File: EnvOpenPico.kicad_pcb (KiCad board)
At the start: 2 copper layers, 21.1 x 51.3 mm, 37 parts, among them J2 B3U-1000P, J3 2.54mm header 01x20, J4 2.54mm header 01x20, J5 Conn_01x03_Male, U1 SPX3819M5-L-3-3, U3 RP2040, X1 XO 32 12Mhz 3225 seiko

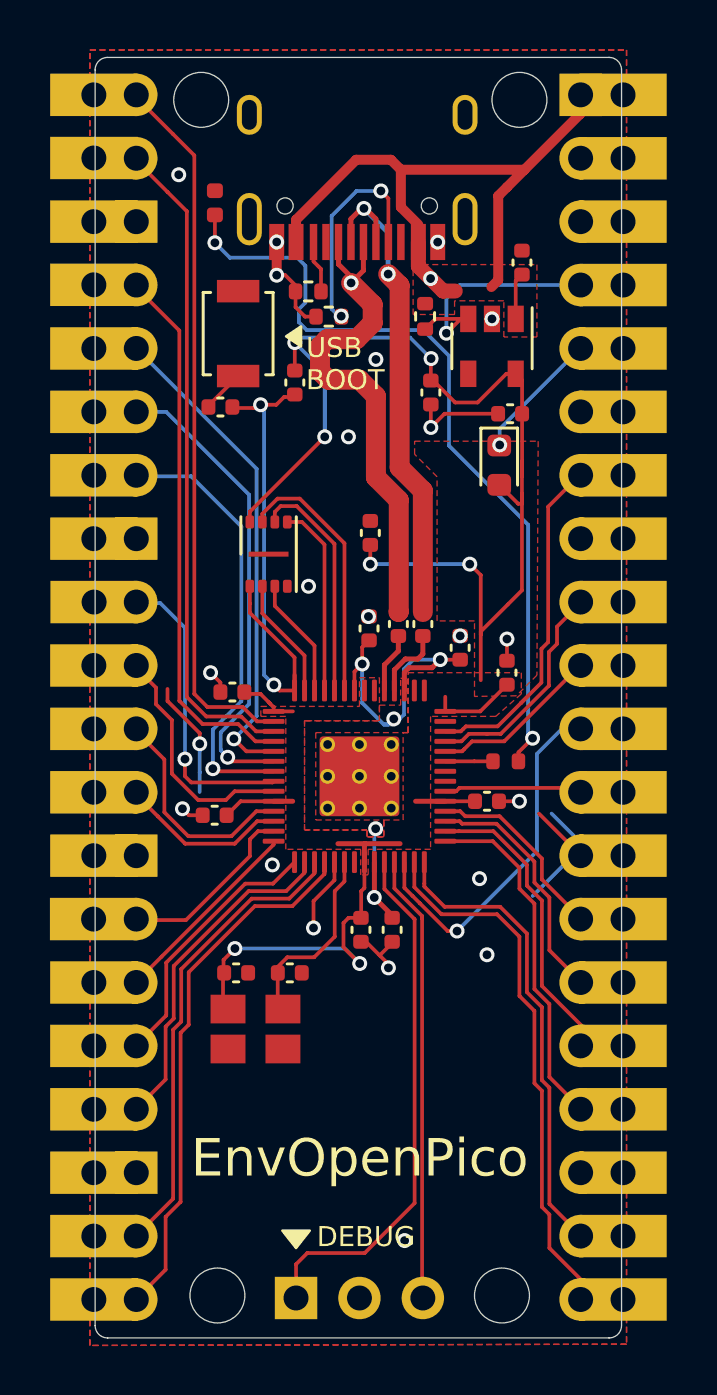
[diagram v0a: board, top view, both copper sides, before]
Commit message: unsure if permanent but can get a hold of components RPI Pico uses
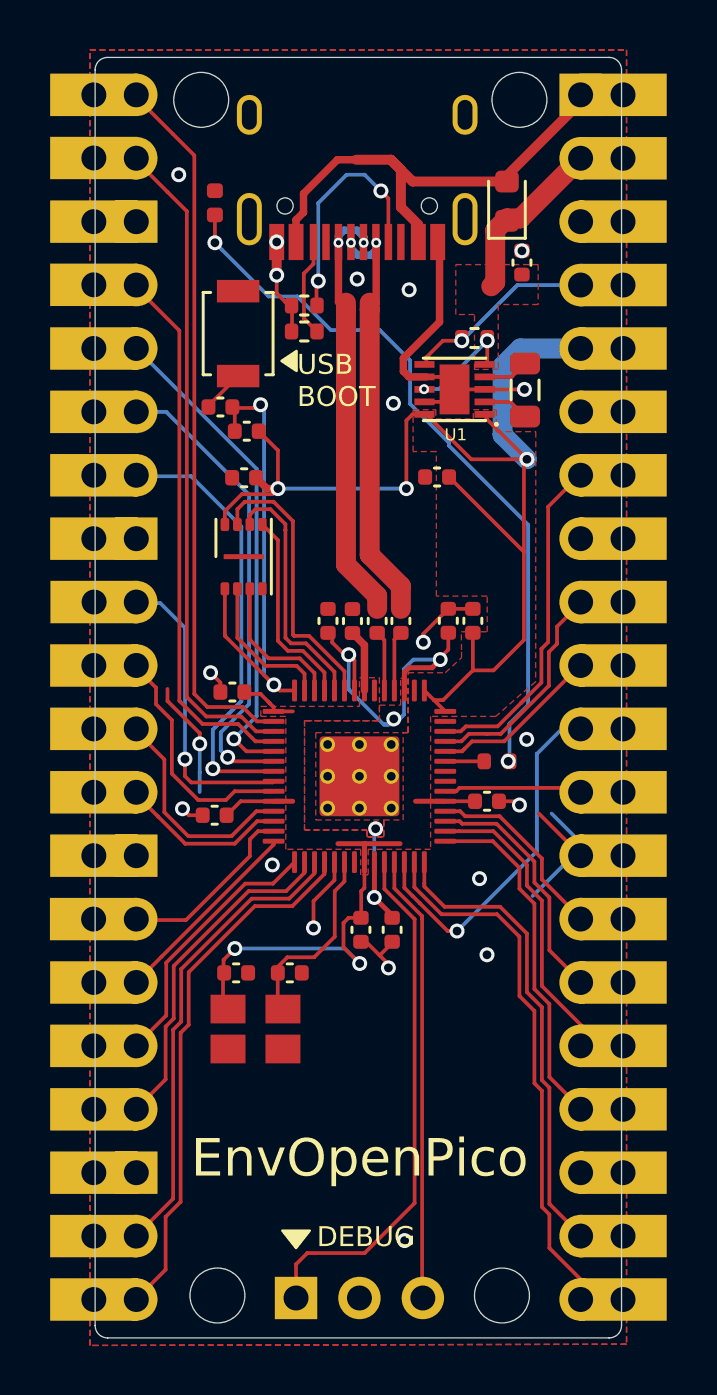
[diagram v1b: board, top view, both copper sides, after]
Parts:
- removed D2: 0603 Diode 1N58, Diode_SMD:D_0603_1608Metric
- added D1: SCHOTTKY DIODE, Diode_SMD:D_0603_1608Metric, F.Cu at (109.6, 63.0)
- added L1: Inductor 2.2uh, Inductor_SMD:L_0805_2012Metric, F.Cu at (110.3, 70.5)
- C1, C17, C4: value 10u -> 10uf 0402
- C10, C3: value 1u -> 1uf 0402
- C11, C13, C14, C15, C5, C6, C7, C8: value 100n -> 100nf 0402
- C2: value 15p -> 15pf 0402
- FLASH1: value W25Q128JVPIQ -> W25Q16JVUXIQ
- R1: value 1k -> 1k Resistor
- R8: value 470 -> 470 ohm resistor
- U1: value SPX3819M5-L-3-3 -> RT6150B-33GQW; footprint Package_TO_SOT_SMD:SOT-23-5 -> RT6150B-33GQW:SON50P250X250X80-11N
- moved C8 9.68 mm to (103.4, 79.8), turned to 90 degrees
- moved C5 5.52 mm to (99.1, 74.1), turned to 180 degrees
- moved C4 3.87 mm to (106.8, 74.0)
- moved R2 2.74 mm to (99.2, 72.2), turned to 180 degrees
- moved C10 2.49 mm to (108.2, 79.8)
- moved U1 2.29 mm to (107.5, 70.5), turned to 180 degrees
- moved R7 2.16 mm to (108.3, 68.5), turned to 180 degrees
- moved C3 1.67 mm to (102.4, 79.8)
- moved R6 1.61 mm to (101.5, 68.2)
- moved C7 1.18 mm to (107.2, 79.8)
- moved R5 1.08 mm to (101.5, 67.2)
- moved FLASH1 1.00 mm to (99.0, 77.2)
- moved R4 0.89 mm to (105.3, 79.8)
- moved R3 0.86 mm to (104.4, 79.8)
- moved R8 0.35 mm to (109.2, 85.4)
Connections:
- J4 pad 2: (no net) -> VBUS
- J4 pad 5: Net-(D2-Pad1) -> +3V3
- J4 pad 6: (no net) -> Net-(J4-Pad6)
- U1 pad 1: VBUS -> +3V3
- U1 pad 2: GND -> Net-(L1-Pad1)
- U1 pad 3: 3V3_EN -> GND
- U1 pad 4: (no net) -> Net-(L1-Pad2)
- U1 pad 5: +3V3 -> VBUS
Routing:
- net GND: track 28.8 -> 39.0 mm, vias 22 -> 20
- net Net-(D2-Pad1): track 5.20 -> 0.00 mm, vias 1 -> 0
- net /USB_D+: track 20.8 -> 17.3 mm, vias 1 -> 2
- net /USB_D-: track 20.3 -> 17.3 mm
- net Net-(D3-Pad2): track 31.9 -> 29.2 mm
- net 3V3_EN: track 10.6 -> 8.26 mm
- net VBUS: track 29.4 -> 31.5 mm, vias 1 -> 2
- net Net-(R6-Pad2): track 2.11 -> 3.98 mm
- net +3V3: track 73.7 -> 75.6 mm, vias 7 -> 5
- net Net-(L1-Pad1): track 0.00 -> 1.79 mm
- net Net-(L1-Pad2): track 0.00 -> 1.77 mm
- net +1V1: track 18.5 -> 19.9 mm
- net /QSPI_SS: track 20.5 -> 19.2 mm
- net /QSPI_SD2: track 4.83 -> 5.88 mm
- net /QSPI_SD1: track 4.88 -> 5.92 mm
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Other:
- rule via_min_size: 0.6 -> 0.4
- board text removed: "3.3V_EN is not implemented"
- board text removed: "VSYS is not implemented"

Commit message: Added some vias and tweaked some placements and adjustments
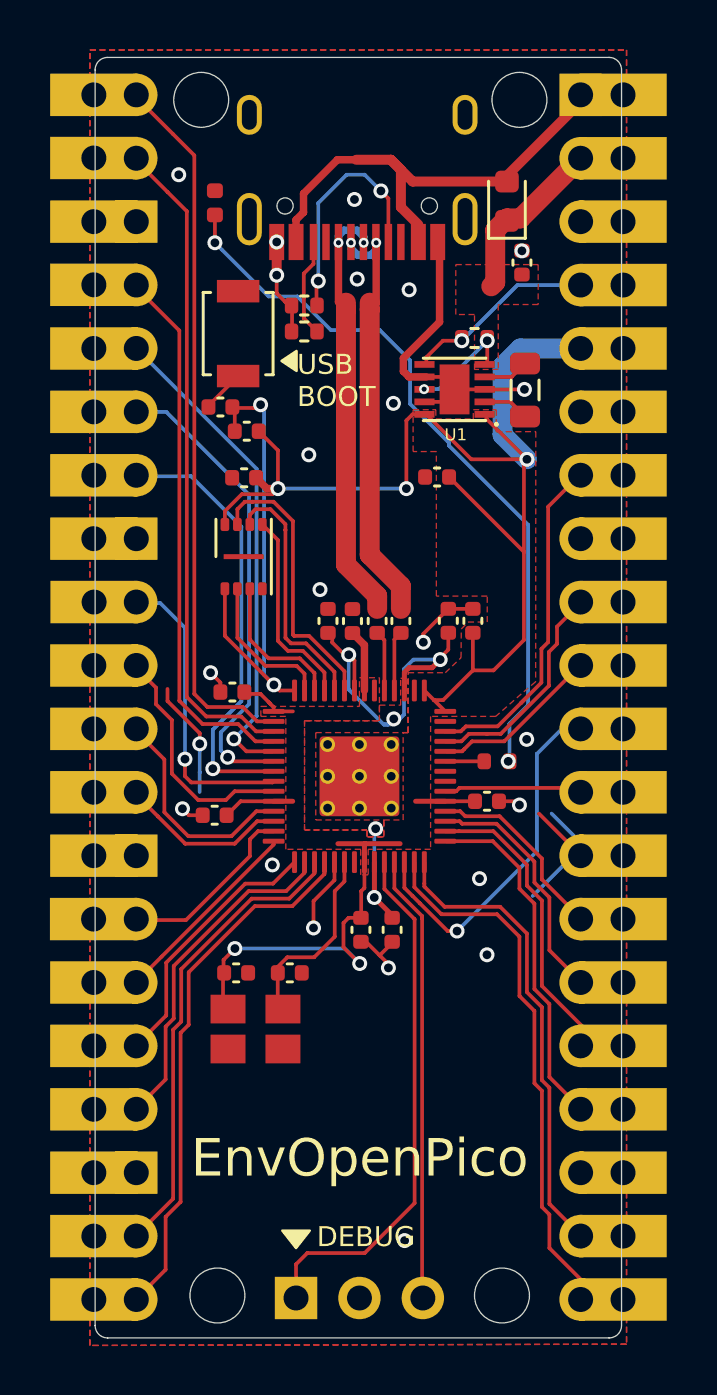
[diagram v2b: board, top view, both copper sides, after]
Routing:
- net GND: vias 20 -> 23

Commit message: Changed out some parts and added more details to their BOM comments
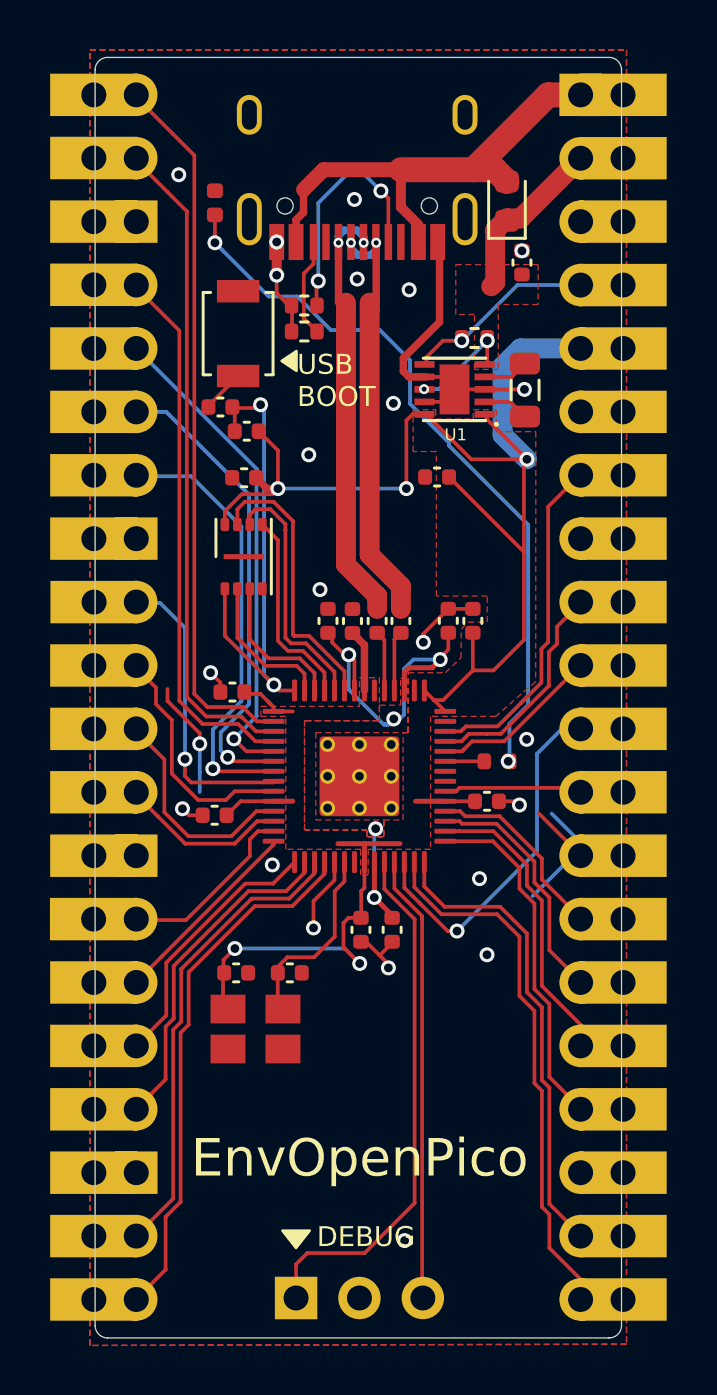
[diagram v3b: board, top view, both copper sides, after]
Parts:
- removed H1, H2, H3, H4: MountingHole, MountingHole:MountingHole_2.2mm_M2
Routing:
- net VBUS: track 31.5 -> 32.1 mm

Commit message: Swapped RT6150GQW for TPS63002
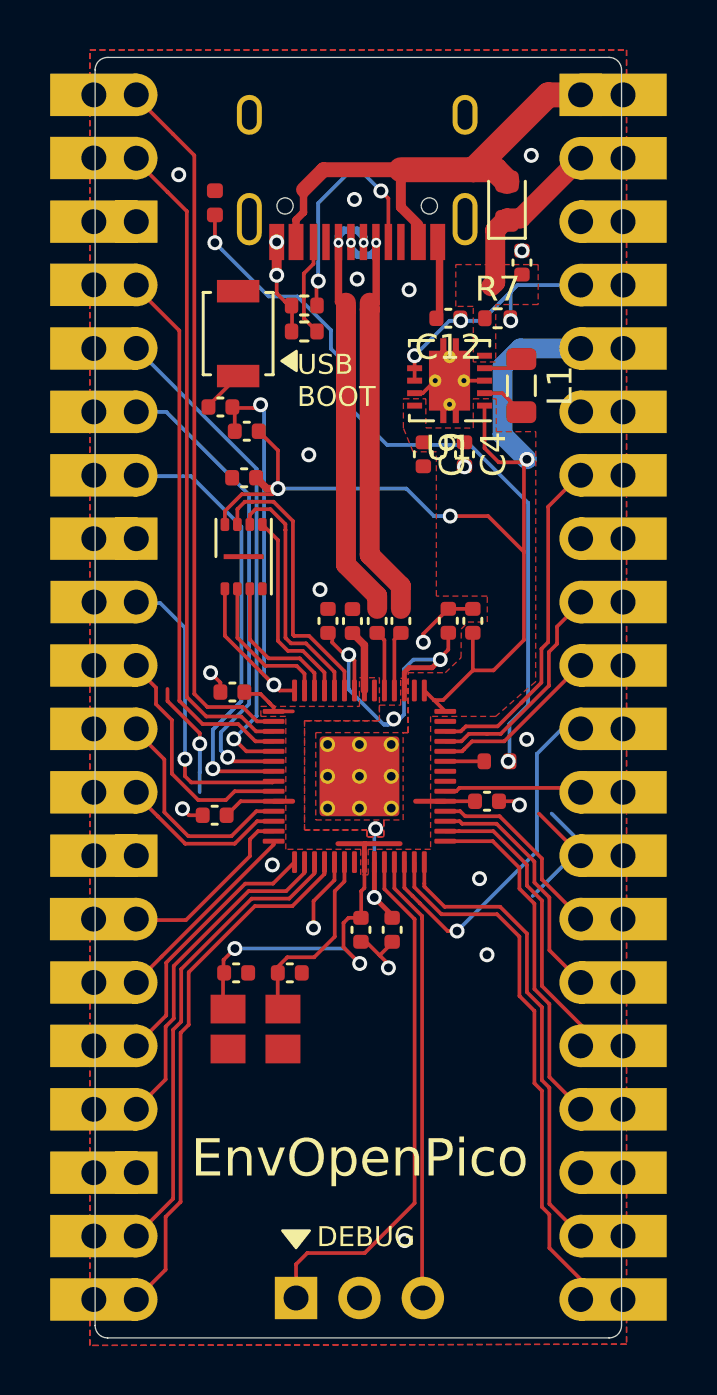
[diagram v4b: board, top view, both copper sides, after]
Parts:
- added C12: 0.1uf 0402, Capacitor_SMD:C_0402_1005Metric, F.Cu at (107.2, 67.7)
- added C9: 10uf 0402, Capacitor_SMD:C_0402_1005Metric, F.Cu at (106.2, 73.1)
- R7: value 100K -> 100ohm
- U1: value RT6150B-33GQW -> TPS63002; footprint RT6150B-33GQW:SON50P250X250X80-11N -> Package_SON:Texas_DRC0010J_ThermalVias
- moved C4 1.43 mm to (107.9, 73.1), turned to 270 degrees
- moved R7 1.22 mm to (109.2, 67.7), turned to 0 degrees
- moved U1 0.40 mm to (107.3, 70.2)
- moved L1 0.23 mm to (110.2, 70.4), turned to 270 degrees
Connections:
- FLASH1 pad 9: (no net) -> Net-(FLASH1-Pad9)
- U1 pad 2: Net-(L1-Pad1) -> Net-(L1-Pad2)
- U1 pad 4: Net-(L1-Pad2) -> Net-(L1-Pad1)
- U1 pad 7: GND -> 3V3_EN
- U1 pad 8: VBUS -> 3V3_EN
- U3 pad 21: (no net) -> /XOUT
- U3 pad 35: (no net) -> /GPIO23
- U3 pad 36: (no net) -> /GPIO24
- U3 pad 41: (no net) -> /GPIO29_ADC3
- X1 pad 1: (no net) -> Net-(X1-Pad1)
- e1 pad 3: (no net) -> Net-(e1-Pad3)
- e1 pad 9: (no net) -> Net-(e1-Pad9)
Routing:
- net GND: track 39.0 -> 32.3 mm
- net +3V3: track 75.6 -> 69.6 mm
- net VBUS: track 32.1 -> 27.8 mm, vias 2 -> 0
- net 3V3_EN: track 8.26 -> 10.7 mm, vias 1 -> 3
- net Net-(D3-Pad2): track 29.2 -> 30.0 mm
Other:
- board text removed: "ADC_VREF is not implemented"

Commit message: Swapped flash chip for larger version, JLCPCB now stocks the RP2040
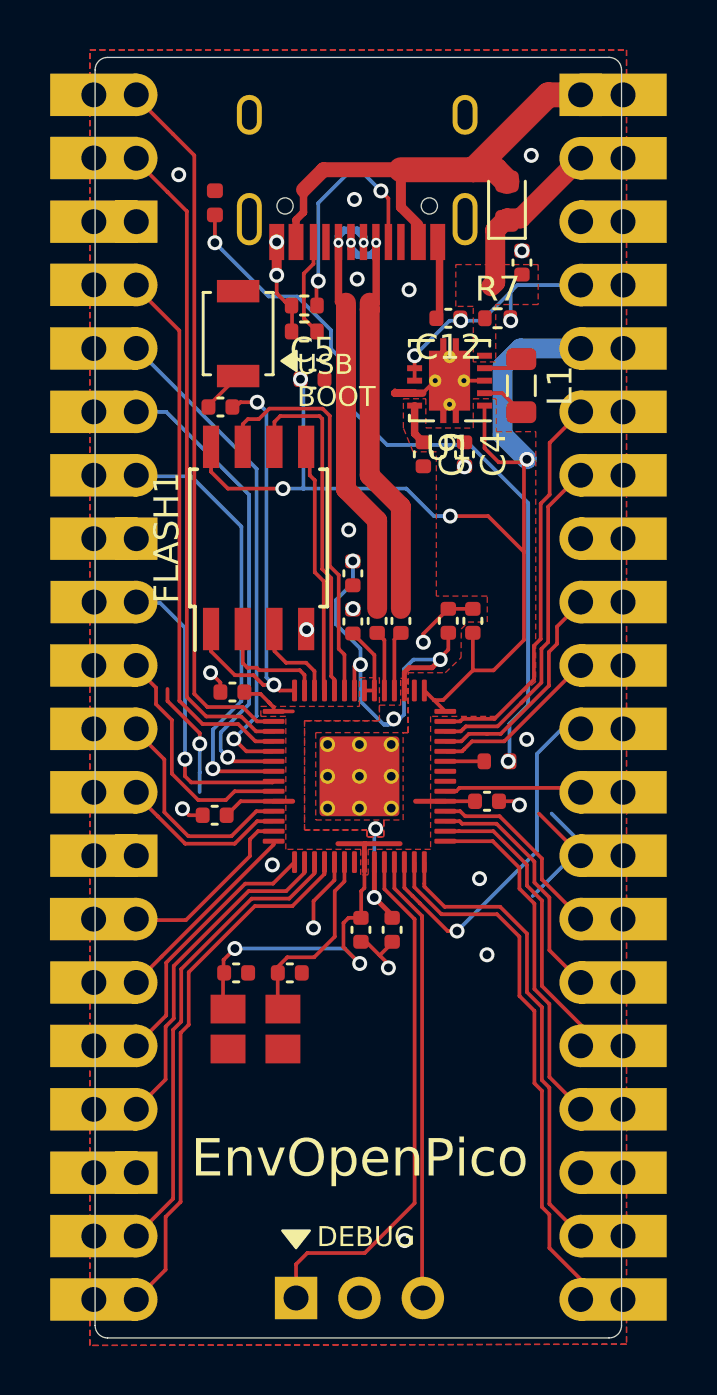
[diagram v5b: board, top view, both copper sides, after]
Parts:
- removed R2: DNF, Capacitor_SMD:C_0402_1005Metric
- FLASH1: value W25Q16JVUXIQ -> W25Q16; footprint Package_SON:SON-8-1EP_3x2mm_P0.5mm_EP1.4x1.6mm -> Package_SO:SOIJ-8_5.3x5.3mm_P1.27mm
- moved C5 4.81 mm to (101.8, 70.1), turned to 0 degrees
- moved C3 2.15 mm to (103.4, 77.9), turned to 270 degrees
- moved FLASH1 0.96 mm to (99.7, 76.5)
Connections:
- J4 pad 6: Net-(J4-Pad6) -> /GPIO29_ADC3
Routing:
- net /GPIO29_ADC3: track 0.00 -> 16.5 mm
- net /QSPI_SD3: track 11.3 -> 16.0 mm
- net +3V3: track 69.6 -> 73.8 mm, vias 5 -> 6
- net /QSPI_SCLK: track 9.98 -> 14.1 mm
- net +1V1: track 19.9 -> 22.6 mm, vias 5 -> 6
- net GND: track 32.3 -> 34.8 mm, vias 23 -> 24
- net /QSPI_SD2: track 5.88 -> 3.60 mm
- net /QSPI_SD0: track 8.03 -> 10.1 mm
- net /QSPI_SS: track 19.2 -> 17.6 mm
- net /QSPI_SD1: track 5.92 -> 4.66 mm

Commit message: Changed button, generated JLCPCB compatible gerbers
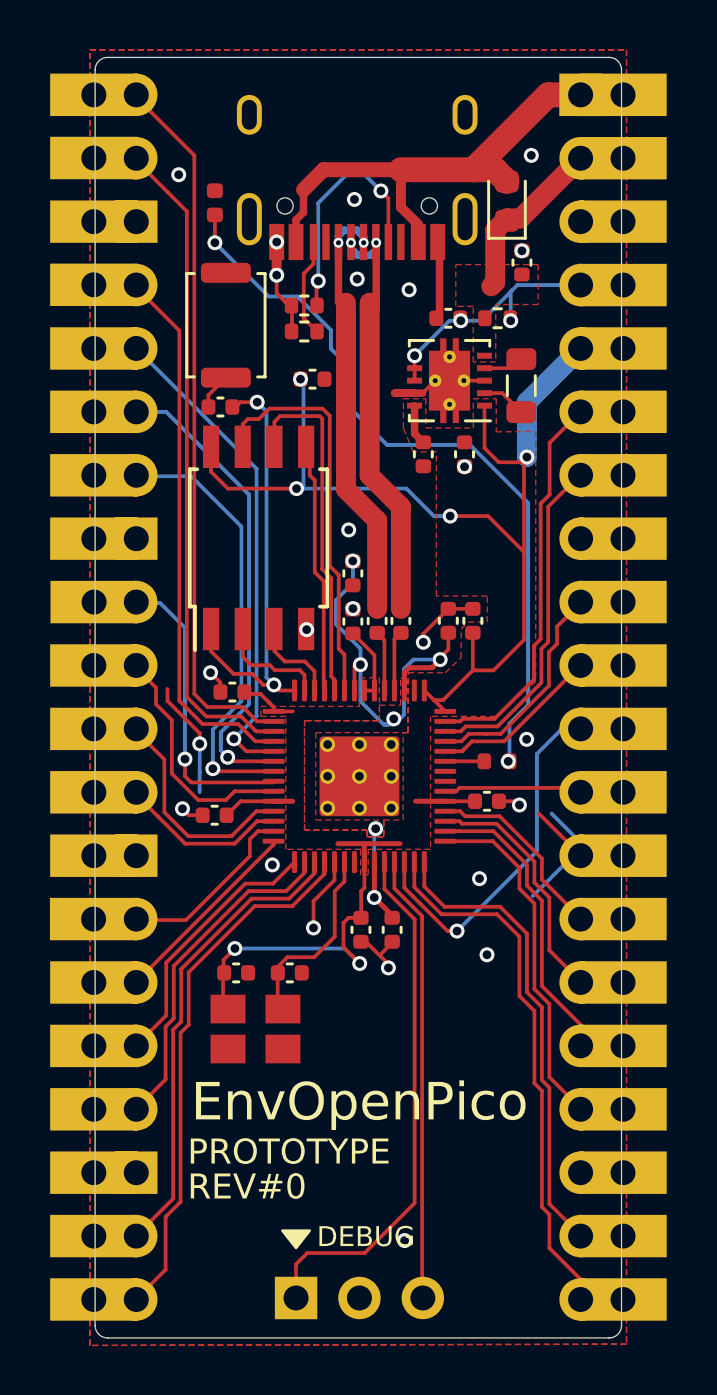
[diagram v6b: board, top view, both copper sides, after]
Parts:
- J2: value B3U-1000P -> SKRKAEE020; footprint Button_Switch_SMD:SW_SPST_B3U-1000P -> Button_Switch_SMD:SW_Push_SPST_NO_Alps_SKRK
- moved J2 0.59 mm to (98.3, 68.0)
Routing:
- net +3V3: track 73.8 -> 71.3 mm
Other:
- board text removed: "USB BOOT"
